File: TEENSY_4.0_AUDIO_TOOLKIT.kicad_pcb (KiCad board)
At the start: 2 copper layers, 100 x 25 mm, 46 parts, among them J1 MIDI_IO1, J14 USB_A, U3 Teensy4.0, U4C1 22 uF, U4C2 0.47uF, U4C3 0.47uF, U4C4 22 uF

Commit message: Added SAI Expansion Headers
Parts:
- added CLK_1: Conn_01x04_Female, Connector_PinSocket_2.54mm:PinSocket_1x04_P2.54mm_Vertical, F.Cu at (208.7, 244.5)
- added CLK_2: Conn_01x04_Female, Connector_PinSocket_2.54mm:PinSocket_1x04_P2.54mm_Vertical, F.Cu at (208.8, 238.7)
- added PWR_1: Conn_01x03_Female, Connector_PinSocket_2.54mm:PinSocket_1x03_P2.54mm_Vertical, F.Cu at (222.0, 239.7)
- added SAI_1: Conn_01x06_Female, Connector_PinSocket_2.54mm:PinSocket_1x06_P2.54mm_Vertical, F.Cu at (208.7, 248.5)
- added SAI_2: Conn_01x03_Female, Connector_PinSocket_2.54mm:PinSocket_1x03_P2.54mm_Vertical, F.Cu at (208.7, 234.7)
- moved D1 18.3 mm to (265.3, 243.5)
- moved 6N137_1 18.3 mm to (262.6, 236.6)
- moved 74LS0 18.3 mm to (245.3, 235.6)
- moved C2 18.3 mm to (226.2, 240.3)
- moved C9 18.3 mm to (236.5, 241.9)
- moved LM2940_3 18.3 mm to (274.2, 247.5)
- moved R38 18.3 mm to (233.3, 241.9)
- moved R5 18.3 mm to (254.0, 232.3)
- moved R6 18.3 mm to (246.4, 242.4)
- moved R8 18.3 mm to (242.7, 242.4)
- moved R9 18.3 mm to (250.2, 242.4)
- moved TPS2055A_1 18.3 mm to (235.1, 236.0)
- moved TX_0 18.3 mm to (254.0, 236.6)
- moved U4C2 18.3 mm to (276.5, 232.0)
- moved U4C3 18.3 mm to (276.9, 242.7)
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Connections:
- U3 pad 10: (no net) -> IN1
- U3 pad 11: (no net) -> OUT1C
- U3 pad 27: (no net) -> LRCLK1
- U3 pad 28: (no net) -> BCLK1
- U3 pad 30: (no net) -> MCLK1
- U3 pad 38: (no net) -> MCLK2
- U3 pad 43: (no net) -> OUT1B
- U3 pad 5: (no net) -> LRCLK2
- U3 pad 6: (no net) -> BCLK2
- U3 pad 8: (no net) -> OUT1D
- U3 pad 9: (no net) -> OUT1A
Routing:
- net 5V: track 114.7 -> 19.4 mm
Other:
- board size 100 x 25 mm -> 115.3 x 25.1 mm
- board text added: "5 3 G"
- board text added: "I A B C D G"
- board text added: "I O G"
- board text added: "M G B L"

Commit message: Update
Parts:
- removed CLK_1, CLK_2: Conn_01x04_Female, Connector_PinSocket_2.54mm:PinSocket_1x04_P2.54mm_Vertical
- removed J1: MIDI_IO1, Connector_PinHeader_2.54mm:PinHeader_2x06_P2.54mm_Vertical
- removed J14: USB_A, TE_USB_A_USBA_292303-4:TE_292303-4
- removed JP1: Barrel_Jack, Connector_BarrelJack:BarrelJack_CUI_PJ-063AH_Horizontal
- removed POWER1: Microfit_power, Connector_Molex:Molex_Micro-Fit_3.0_43045-0412_2x02_P3.00mm_Vertical
- removed PWR_1, SAI_2: Conn_01x03_Female, Connector_PinSocket_2.54mm:PinSocket_1x03_P2.54mm_Vertical
- removed SAI_1: Conn_01x06_Female, Connector_PinSocket_2.54mm:PinSocket_1x06_P2.54mm_Vertical
- removed TOS_IN0: EAPLRAA4, PLR135-T10_PLT133-T10W
- removed TOS_O0: PLT133-T10W, PLT133-T10W:PLR135-T10_PLT133-T10W
- added MCLK1: MCLK1, project_fp:SolderWirePad_1x01_THROUGH_SOLDER, F.Cu at (180.8, 232.8)
- added MCLK2: MCLK2, project_fp:SolderWirePad_1x01_THROUGH_SOLDER, F.Cu at (186.1, 232.8)
- added MIDI_IO1: MIDI_IO1, project_fp:PinHeader_2x06_P2.54mm_Vertical, F.Cu at (225.5, 91.6)
- added POWER_IN1: Conn_02x02_Odd_Even, project_fp:PinHeader_2x02_P2.54mm_Vertical, F.Cu at (48.6, 96.5)
- added POWER_IO2: Barrel_Jack, project_fp:BarrelJack_CUI_PJ-063AH_Horizontal, F.Cu at (56.4, 140.7)
- added POWER_IO3: Microfit_power, project_fp:Molex_Micro-Fit_3.0_43045-0412_2x02_P3.00mm_Vertical, F.Cu at (70.2, 92.8)
- added POWER_OUT1: Conn_02x02_Odd_Even, project_fp:PinHeader_2x02_P2.54mm_Vertical, F.Cu at (58.4, 95.9)
- added R10: 2.2K, Resistor_SMD:R_0603_1608Metric_Pad1.05x0.95mm_HandSolder, F.Cu at (204.6, 231.1)
- added R11: 2.2K, Resistor_SMD:R_0603_1608Metric_Pad1.05x0.95mm_HandSolder, F.Cu at (204.6, 229.4)
- added R12: 100 Ohm, Resistor_SMD:R_0603_1608Metric_Pad1.05x0.95mm_HandSolder, F.Cu at (186.1, 234.6)
- added R3: 220R, Resistor_SMD:R_0603_1608Metric_Pad1.05x0.95mm_HandSolder, F.Cu at (244.8, 239.5)
- added R4: 100 Ohm, Resistor_SMD:R_0603_1608Metric_Pad1.05x0.95mm_HandSolder, F.Cu at (180.9, 234.4)
- added TOS_IN1: EAPLRAA4, project_fp:PLR135-T10_PLT133-T10W, F.Cu at (311.5, 140.9)
- added TOS_OUT1: PLT133-T10W, project_fp:PLR135-T10_PLT133-T10W, F.Cu at (323.1, 140.4)
- added USB_A1: USB_A, project_fp:TE_292303-4, F.Cu at (111.4, 141.9)
- 6N137_1: footprint Package_DIP:DIP-8_W7.62mm_SMDSocket_SmallPads -> project_fp:DIP-8_W7.62mm_SMDSocket_SmallPads
- IO_1, IO_2: footprint Connector_PinHeader_2.54mm:PinHeader_2x15_P2.54mm_Vertical -> project_fp:PinHeader_2x18_P2.54mm_Vertical
- MEM1: footprint project_fp:23LC1024-I&slash_ST -> project_fp:23LC1024
- SD1: value DM3D-SF -> DM3D-SF-Hirose; footprint DM3D-SF:DM3D-SF -> project_fp:DM3D-SF
- SPDIF_IO1: footprint Connector_PinHeader_2.54mm:PinHeader_2x03_P2.54mm_Vertical -> project_fp:PinHeader_2x03_P2.54mm_Vertical
- TPS2055A_1: value TPS2055A -> TPS2055A-TPS2055A; footprint Package_SO:SOIC-8_3.9x4.9mm_P1.27mm -> project_fp:SOIC-8_3.9x4.9mm_P1.27mm
- U3: footprint teensy:Teensy40_SMT -> project_fp:Teensy40_SMT_Audio_Kit_2
- USB_IO1: value USB_Header -> USB_Header_5_Pin-USB_Header; footprint Connector_PinHeader_2.54mm:PinHeader_1x05_P2.54mm_Vertical -> project_fp:PinHeader_1x05_P2.54mm_Vertical
- moved U3 26.2 mm to (165.0, 225.0)
- moved 6N137_1 15.4 mm to (247.7, 232.7)
- moved 74LS0 15.4 mm to (230.5, 231.7)
- moved C2 15.4 mm to (211.3, 236.4)
- moved D1 15.4 mm to (250.4, 239.7)
- moved LM2940_3 15.4 mm to (259.3, 243.6)
- moved R38 15.4 mm to (218.5, 238.1)
- moved R5 15.4 mm to (239.1, 228.5)
- moved TPS2055A_1 15.4 mm to (220.2, 232.1)
- moved TX_0 15.4 mm to (239.2, 232.7)
- moved U4C2 15.4 mm to (261.6, 228.1)
- moved U4C3 15.4 mm to (262.0, 238.8)
- moved U4C4 15.4 mm to (258.5, 238.8)
- moved R6 15.4 mm to (231.6, 238.6)
- moved R8 15.4 mm to (227.8, 238.6)
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- renumbered SPDIF_OUT0 to SPDIF_OUT1
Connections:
- 6N137_1 pad 2: MIDI_IN_5 -> Net-(6N137_1-Pad2)
- 6N137_1 pad 3: MIDI_IN_4 -> MIDI_IN_5
- C9 pad 1: Net-(C9-Pad1) -> 5V_TPS2055A
- D1 pad 1: MIDI_IN_4 -> Net-(6N137_1-Pad2)
- IO_1 pad 10: (no net) -> GND
- IO_1 pad 11: GND -> USB_D-
- IO_1 pad 12: (no net) -> GND
- IO_1 pad 13: (no net) -> USB_D+
- IO_1 pad 14: (no net) -> GND
- IO_1 pad 15: SPDIF_OUT -> GND
- IO_1 pad 16: (no net) -> GND
- IO_1 pad 17: SPDIF_IN -> (no net)
- IO_1 pad 18: (no net) -> GND
- IO_1 pad 19: 3.3V -> SPDIF_OUT
- IO_1 pad 2: (no net) -> GND
- IO_1 pad 20: (no net) -> GND
- IO_1 pad 21: MIDI_IN_4 -> SPDIF_IN
- IO_1 pad 22: (no net) -> GND
- IO_1 pad 23: MIDI_IN_5 -> 3.3V
- IO_1 pad 24: (no net) -> GND
- IO_1 pad 25: MIDI_OUT_4 -> MIDI_IN_4
- IO_1 pad 26: (no net) -> GND
- IO_1 pad 27: MIDI_OUT_5 -> MIDI_IN_5
- IO_1 pad 28: (no net) -> GND
- IO_1 pad 29: MIDI_THRU_4 -> MIDI_OUT_4
- IO_1 pad 30: (no net) -> GND
- IO_1 pad 4: (no net) -> GND
- IO_1 pad 6: (no net) -> GND
- IO_1 pad 7: USB_D- -> 3.3V
- IO_1 pad 8: (no net) -> GND
- IO_1 pad 9: USB_D+ -> 5V_TPS2055A
- IO_2 pad 1: 12V -> 12V_H
- IO_2 pad 10: (no net) -> GND_H
- IO_2 pad 11: GND -> USB_D-_H
- IO_2 pad 12: (no net) -> GND_H
- IO_2 pad 13: (no net) -> USB_D+_H
- IO_2 pad 14: (no net) -> GND_H
- IO_2 pad 15: SPDIF_OUT -> GND_H
- IO_2 pad 16: (no net) -> GND_H
- IO_2 pad 17: SPDIF_IN -> (no net)
- IO_2 pad 18: (no net) -> GND_H
- IO_2 pad 19: 3.3V -> SPDIF_OUT_H
- IO_2 pad 2: (no net) -> GND_H
- IO_2 pad 20: (no net) -> GND_H
- IO_2 pad 21: MIDI_IN_4 -> SPDIF_IN_H
- IO_2 pad 22: (no net) -> GND_H
- IO_2 pad 23: MIDI_IN_5 -> 3.3V_H
- IO_2 pad 24: (no net) -> GND_H
- IO_2 pad 25: MIDI_OUT_4 -> MIDI_IN_4_H
- IO_2 pad 26: (no net) -> GND_H
- IO_2 pad 27: MIDI_OUT_5 -> MIDI_IN_5_H
- IO_2 pad 28: (no net) -> GND_H
- IO_2 pad 29: MIDI_THRU_4 -> MIDI_OUT_4_H
- IO_2 pad 3: 12V -> 12V_H
- IO_2 pad 30: (no net) -> GND_H
- IO_2 pad 4: (no net) -> GND_H
- IO_2 pad 5: 5V -> (no net)
- IO_2 pad 6: (no net) -> GND_H
- IO_2 pad 7: USB_D- -> 3.3V_H
- IO_2 pad 8: (no net) -> GND_H
- IO_2 pad 9: USB_D+ -> 5V_TPS2055A_H
- LM2940_3 pad 1: GND -> (no net)
- MIDI_IN_1 pad 2: MIDI_IN_5 -> GND_H
- MIDI_IN_1 pad 4: MIDI_IN_4 -> MIDI_IN_4_H
- MIDI_IN_1 pad 5: (no net) -> MIDI_IN_5_H
- MIDI_IN_2 pad 1: (no net) -> MIDI_IN_4_H
- MIDI_IN_2 pad 2: (no net) -> GND_H
- MIDI_IN_2 pad 3: (no net) -> MIDI_IN_5_H
- MIDI_OUT_1 pad 2: GND -> GND_H
- MIDI_OUT_1 pad 4: MIDI_OUT_4 -> MIDI_OUT_4_H
- MIDI_OUT_1 pad 5: MIDI_OUT_5 -> MIDI_OUT_5_H
- MIDI_OUT_2 pad 1: (no net) -> MIDI_THRU_4_H
- MIDI_OUT_2 pad 2: (no net) -> GND_H
- MIDI_OUT_2 pad 3: (no net) -> MIDI_THRU_5_H
- MIDI_THROUGH_1 pad 2: GND -> GND_H
- MIDI_THROUGH_1 pad 4: MIDI_THRU_4 -> MIDI_THRU_4_H
- MIDI_THROUGH_1 pad 5: MIDI_THRU_5 -> MIDI_THRU_5_H
- MIDI_THROUGH_2 pad 1: (no net) -> MIDI_OUT_4_H
- MIDI_THROUGH_2 pad 2: (no net) -> GND_H
- MIDI_THROUGH_2 pad 3: (no net) -> MIDI_OUT_5_H
- R1 pad 1: Net-(R1-Pad1) -> SPDIF_IN
- R2 pad 1: Net-(R1-Pad1) -> SPDIF_IN
- R23 pad 1: Net-(R23-Pad1) -> SPDIF_OUT
- R24 pad 1: Net-(R23-Pad1) -> SPDIF_OUT
- SPDIF_IN1 pad 1: (no net) -> GND_H
- SPDIF_IN1 pad 2: (no net) -> SPDIF_IN_H
- SPDIF_IO1 pad 1: Net-(R23-Pad1) -> SPDIF_OUT_H
- SPDIF_IO1 pad 2: GND -> GND_H
- SPDIF_IO1 pad 3: Net-(R1-Pad1) -> SPDIF_IN_H
- SPDIF_IO1 pad 4: GND -> GND_H
- SPDIF_IO1 pad 5: 3.3V -> SPDIF_3.3V_H
- SPDIF_IO1 pad 6: GND -> GND_H
- SPDIF_OUT1 pad 1: (no net) -> GND_H
- SPDIF_OUT1 pad 2: (no net) -> SPDIF_OUT_H
- TPS2055A_1 pad 6: Net-(C9-Pad1) -> 5V_TPS2055A
- TPS2055A_1 pad 7: Net-(C9-Pad1) -> 5V_TPS2055A
- TPS2055A_1 pad 8: Net-(C9-Pad1) -> 5V_TPS2055A
- U3 pad 10: IN1 -> (no net)
- U3 pad 11: OUT1C -> (no net)
- U3 pad 17: (no net) -> GND
- U3 pad 25: (no net) -> SDA0
- U3 pad 26: (no net) -> SCL0
- U3 pad 27: LRCLK1 -> (no net)
- U3 pad 28: BCLK1 -> (no net)
- U3 pad 43: OUT1B -> (no net)
- U3 pad 5: LRCLK2 -> (no net)
- U3 pad 6: BCLK2 -> (no net)
- U3 pad 8: OUT1D -> (no net)
- U3 pad 9: OUT1A -> (no net)
- U4C3 pad 2: GND -> (no net)
- U4C4 pad 2: GND -> (no net)
- USB_IO1 pad 1: Net-(C9-Pad1) -> 5V_TPS2055A_H
- USB_IO1 pad 2: USB_D- -> USB_D-_H
- USB_IO1 pad 3: USB_D+ -> USB_D+_H
- USB_IO1 pad 4: Net-(J14-Pad4) -> GND_H
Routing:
- net GND: track 202.0 -> 104.1 mm
- net 3.3V: track 95.8 -> 0.00 mm
- net 5V: track 19.4 -> 13.2 mm
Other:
- board size 115.3 x 25.1 mm -> 100 x 25 mm
- board text added: "DC BARREL"
- board text added: "I2C"
- board text added: "PLUS... - SOLDER PADS FOR SAI - MASTER CLOCK RESISTOR - I2C PULL UPS - SD CARD - RAM/MEMORY"
- board text added: "POWER HEADERS"
- board text removed: "5 3 G"
- board text removed: "I A B C D G"
- board text removed: "I O G"
- board text removed: "M G B L"
- board text removed: "MICROFIT POWER"
- board text removed: "PLUS... SD CARD & RAM/MEMORY ON BOARD"
- board text removed: "POWER"

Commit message: Update
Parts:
- added C3: .1 uF, Capacitor_SMD:C_0603_1608Metric, F.Cu at (224.6, 229.6)
- added R13: 470, Resistor_SMD:R_0603_1608Metric_Pad1.05x0.95mm_HandSolder, F.Cu at (224.5, 233.5)
- R6, R9: value 47 -> 220
- moved C2 5.62 mm to (207.0, 240.0)
- moved C1 5.62 mm to (207.1, 235.3)
- moved R1 5.62 mm to (209.7, 234.5)
- moved R2 5.62 mm to (209.7, 236.3)
- moved R23 5.62 mm to (209.7, 239.2)
- moved R24 5.62 mm to (209.7, 240.9)
- moved R10 3.76 mm to (208.4, 231.5)
- moved R11 3.76 mm to (208.3, 229.8)
- moved C9 2.29 mm to (219.4, 237.8)
- moved R38 2.29 mm to (216.2, 237.8)
- moved TPS2055A_1 2.29 mm to (217.9, 231.8)
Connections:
- 6N137_1 pad 6: 5V -> MIDI_RX
- 74LS0 pad 1: 5V -> MIDI_RX
- 74LS0 pad 12: Net-(74LS0-Pad12) -> MIDI_TX
- 74LS0 pad 13: Net-(74LS0-Pad12) -> MIDI_TX
- 74LS0 pad 2: 5V -> MIDI_RX
- 74LS0 pad 7: (no net) -> GND
- IO_2 pad 5: (no net) -> 5V_H
- LM2940_3 pad 1: (no net) -> GND
- MIDI_IO1 pad 1: (no net) -> MIDI_IN_4_H
- MIDI_IO1 pad 11: (no net) -> MIDI_THRU_5_H
- MIDI_IO1 pad 3: (no net) -> MIDI_IN_5_H
- MIDI_IO1 pad 5: (no net) -> MIDI_OUT_4_H
- MIDI_IO1 pad 7: (no net) -> MIDI_OUT_5_H
- MIDI_IO1 pad 9: (no net) -> MIDI_THRU_4_H
- POWER_IN1 pad 1: (no net) -> 12V_H
- POWER_IN1 pad 3: (no net) -> 12V_H
- POWER_OUT1 pad 1: (no net) -> 5V_H
- POWER_OUT1 pad 3: (no net) -> 3.3V_H
- R2 pad 2: (no net) -> GND
- R24 pad 2: (no net) -> GND
- RX_0 pad 2: 5V -> MIDI_RX
- U3 pad 2: 5V -> MIDI_RX
- U4C3 pad 2: (no net) -> GND
- U4C4 pad 2: (no net) -> GND
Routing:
- net Net-(74LS0-Pad8): track 18.2 -> 0.00 mm
- net 5V: track 13.2 -> 0.00 mm
- net Net-(74LS0-Pad6): track 9.65 -> 0.00 mm
- net Net-(BYPASS_MIDI_TX_1-Pad1): track 8.97 -> 0.00 mm
- net Net-(R9-Pad2): track 1.38 -> 0.00 mm

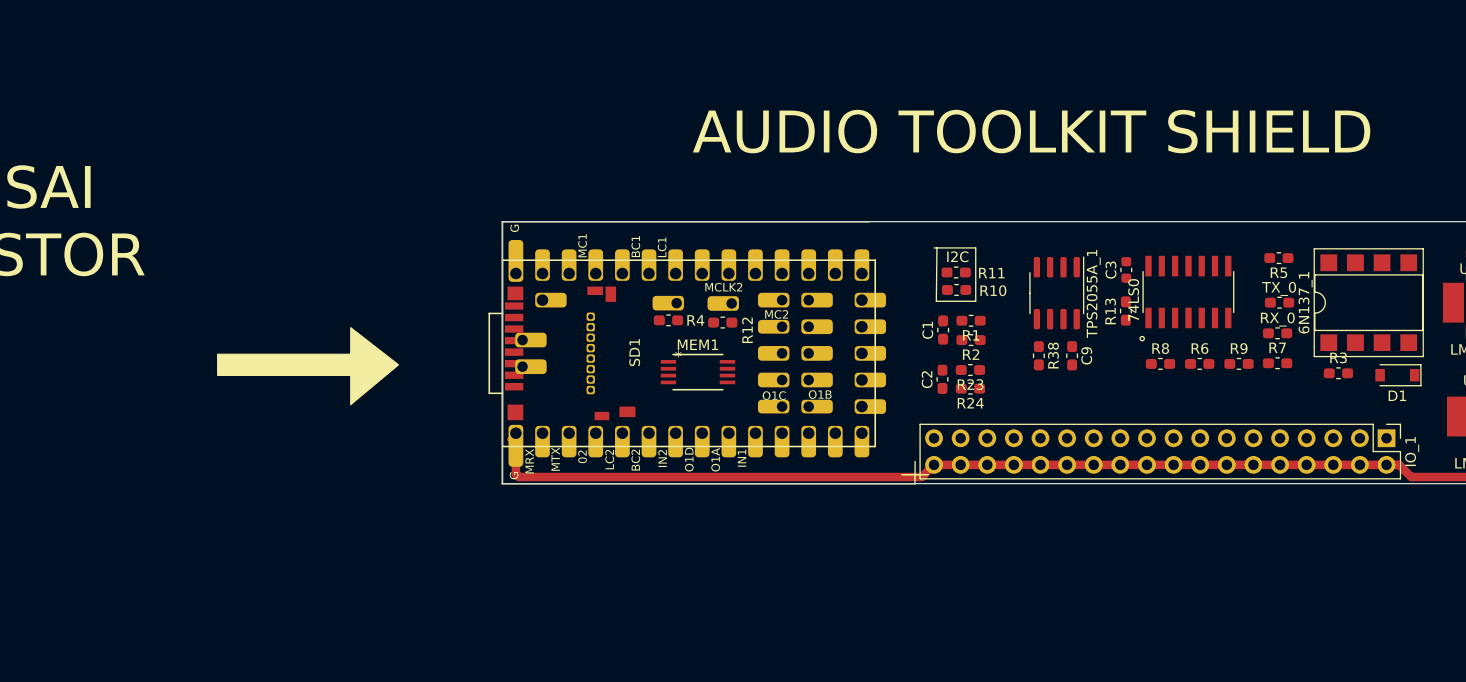
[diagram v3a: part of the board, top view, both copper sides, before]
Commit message: Added labels to IO
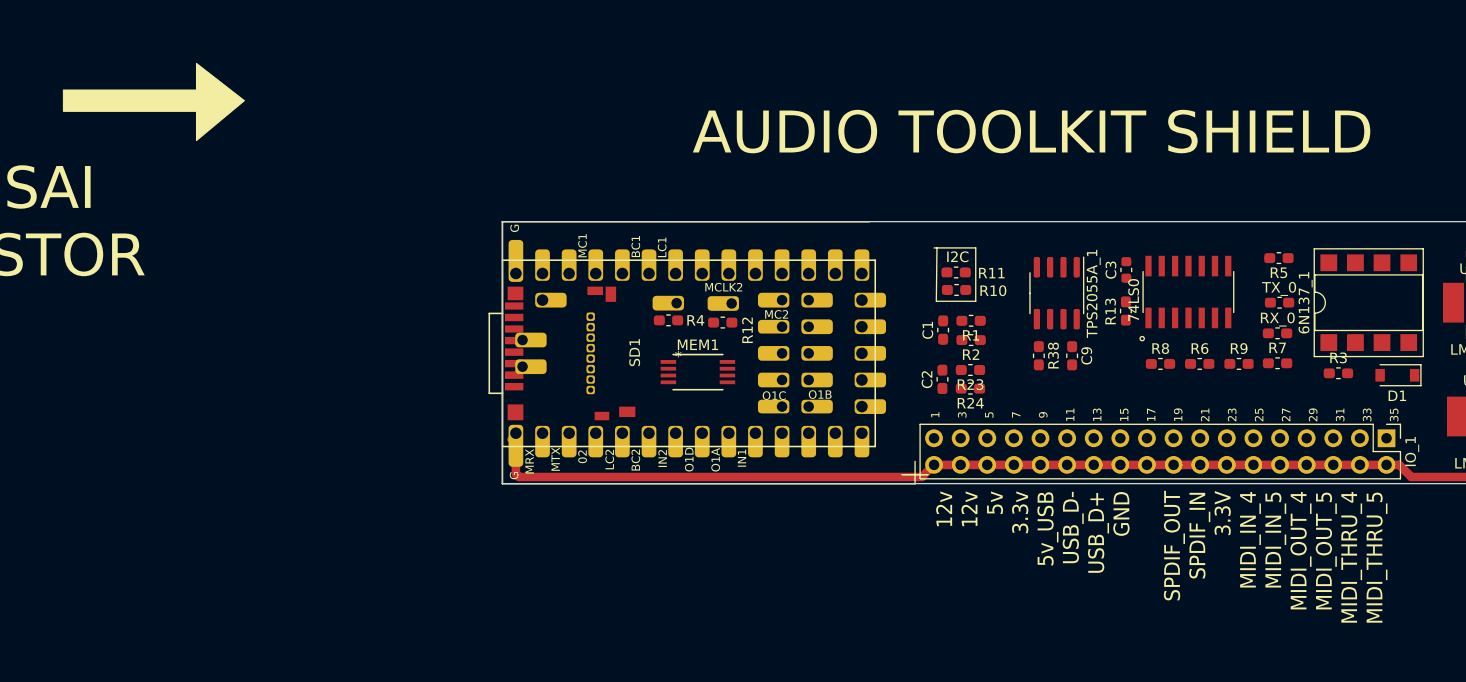
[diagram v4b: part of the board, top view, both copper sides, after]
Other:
- board text added: "1 3 5 7 9 11 13 15 17 19 21 23 25 27 29 31 33 35"
- board text added: "12v 12v 5v 3.3v 5v_USB USB_D- USB_D+ GND SPDIF_OUT SPDIF_IN 3.3V MIDI_IN_4 MIDI_IN_5 MIDI_OUT_4 MIDI_OUT_5 MIDI_THRU_4 MIDI_THRU_5"
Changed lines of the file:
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@@
   (general
     (thickness 1.6)
-    (drawings 29)
+    (drawings 32)
     (tracks 10)
     (zones 0)
@@
     )
   )
+  (gr_text "1\n\n3\n\n5\n\n7\n\n9\n\n11\n\n13\n\n15\n\n17\n\n19\n\n21\n\n23\n\n25\n\n27\n\n29\n\n31\n\n33\n\n35" (at 228.25 243.44 90) (layer F.SilkS)
+    (effects (font (size 0.8 0.8) (thickness 0.125)))
+  )
+  (gr_text "12v\n12v\n5v\n3.3v\n5v_USB\nUSB_D-\nUSB_D+\nGND\n\nSPDIF_OUT\nSPDIF_IN\n3.3V\nMIDI_IN_4\nMIDI_IN_5\nMIDI_OUT_4\nMIDI_OUT_5\nMIDI_THRU_4\nMIDI_THRU_5" (at 227.98 243.78 270) (layer B.SilkS)
+    (effects (font (size 1.5 1.4) (thickness 0.3)) (justify left mirror))
+  )
+  (gr_text "12v\n12v\n5v\n3.3v\n5v_USB\nUSB_D-\nUSB_D+\nGND\n\nSPDIF_OUT\nSPDIF_IN\n3.3V\nMIDI_IN_4\nMIDI_IN_5\nMIDI_OUT_4\nMIDI_OUT_5\nMIDI_THRU_4\nMIDI_THRU_5" (at 227.77 250.69 90) (layer F.SilkS)
+    (effects (font (size 1.5 1.4) (thickness 0.3)) (justify right))
+  )
   (gr_text "PLUS...\n - SOLDER PADS FOR SAI\n - MASTER CLOCK RESISTOR\n - I2C PULL UPS\n - SD CARD\n - RAM/MEMORY" (at 92.28 231.5) (layer F.SilkS)
     (effects (font (size 4 4) (thickness 1)))
@@
     (effects (font (size 4 4) (thickness 1)))
   )
-  (gr_poly (pts (xy 150.544 237.648) (xy 150.544 235.108) (xy 155.116 238.664) (xy 150.544 242.474) (xy 150.544 239.68) (xy 137.844 239.68) (xy 137.844 237.648)) (layer F.SilkS) (width 0.1))
+  (gr_poly (pts (xy 135.83 212.44) (xy 135.83 209.9) (xy 140.402 213.456) (xy 135.83 217.266) (xy 135.83 214.472) (xy 123.13 214.472) (xy 123.13 212.44)) (layer F.SilkS) (width 0.1))
   (gr_text "AUDIO TOOLKIT SHIELD" (at 215.66 216.55) (layer F.SilkS)
     (effects (font (size 4 4) (thickness 1)))

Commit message: Update
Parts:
- moved R38 30.1 mm to (246.3, 238.2)
- moved C9 30.1 mm to (249.5, 238.2)
- moved TPS2055A_1 30.1 mm to (248.1, 232.2)
- moved 6N137_1 10.0 mm to (237.7, 232.8)
- moved D1 10.0 mm to (240.4, 239.8)
- moved R13 10.0 mm to (214.5, 233.6)
- moved R3 10.0 mm to (234.8, 239.6)
- moved R7 10.0 mm to (229.0, 238.6)
- moved R9 10.0 mm to (225.3, 238.7)
- moved RX_0 10.0 mm to (229.0, 235.8)
- moved 74LS0 10.0 mm to (220.4, 231.8)
- moved C3 10.0 mm to (214.5, 229.7)
- moved R5 10.0 mm to (229.1, 228.6)
- moved R6 10.0 mm to (221.5, 238.7)
- moved R8 10.0 mm to (217.8, 238.7)
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
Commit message: Update
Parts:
- added R14: 220R, Resistor_SMD:R_0603_1608Metric_Pad1.05x0.95mm_HandSolder, F.Cu at (170.9, 222.6)
- SD1: moved to B.Cu
- turned SD1 to 90 degrees
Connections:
- U3 pad 38: MCLK2 -> (no net)
- U3 pad 43: (no net) -> OUT1B
- U3 pad 44: (no net) -> MCLK2

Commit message: Update
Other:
- board text added: "<GND"
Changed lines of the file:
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@@
   (general
     (thickness 1.6)
-    (drawings 33)
+    (drawings 35)
     (tracks 10)
     (zones 0)
@@
     (35 F.Paste user hide)
     (36 B.SilkS user hide)
-    (37 F.SilkS user hide)
+    (37 F.SilkS user)
     (38 B.Mask user hide)
     (39 F.Mask user hide)
@@
     )
   )
+  (gr_text <GND (at 203.8604 247.7389 90) (layer F.SilkS)
+    (effects (font (size 0.8 0.8) (thickness 0.18)))
+  )
+  (gr_poly (pts (xy 204.9145 249.2629) (xy 250.7869 249.2629) (xy 250.7615 249.9487) (xy 204.9145 249.9741) (xy 204.9018 249.2375) (xy 204.9018 249.2248)) (layer F.SilkS) (width 0.1))
   (gr_text "1\n\n3\n\n5\n\n7\n\n9\n\n11\n\n13\n\n15\n\n17\n\n19\n\n21\n\n23\n\n25\n\n27\n\n29\n\n31\n\n33\n\n35" (at 227.92 242.82 270) (layer B.SilkS)
     (effects (font (size 0.76 0.8) (thickness 0.125)) (justify mirror))
